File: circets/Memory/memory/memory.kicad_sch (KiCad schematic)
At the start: 29 parts

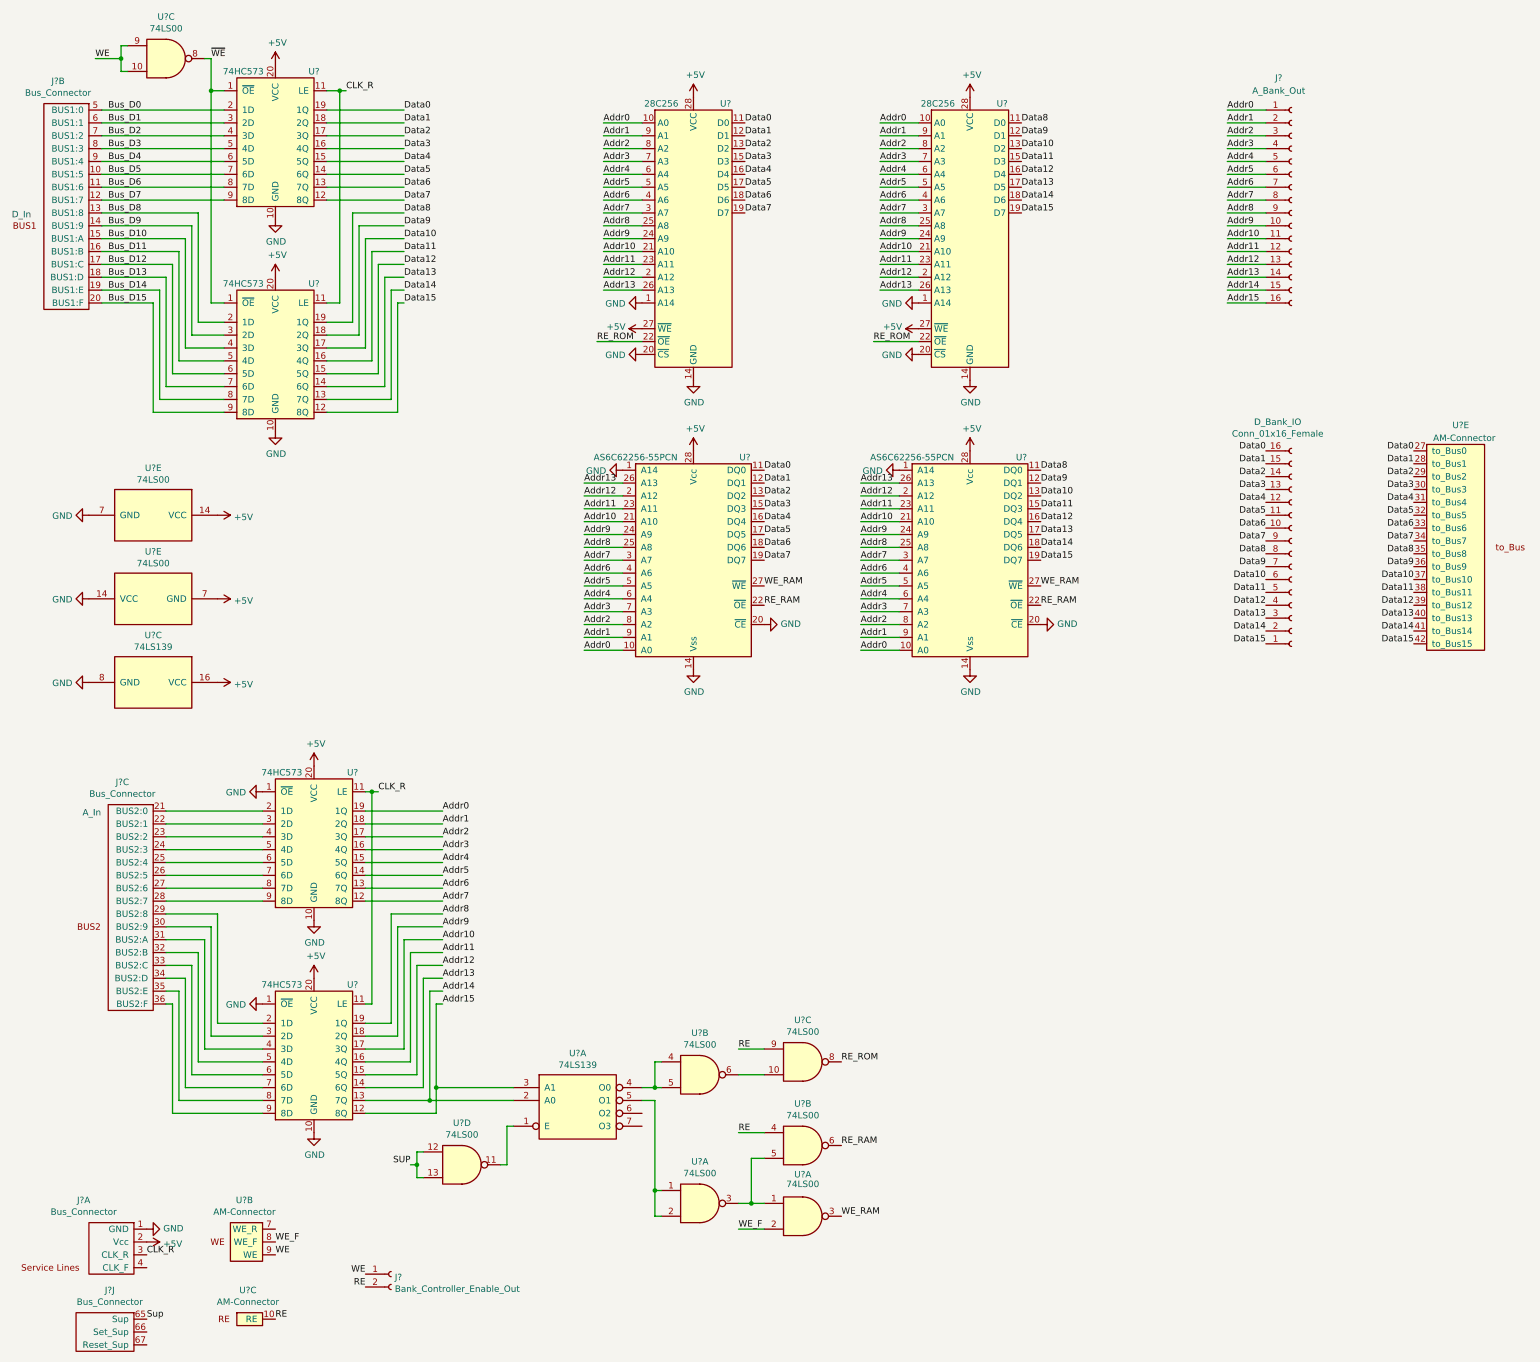
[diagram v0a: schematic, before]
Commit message: Build PCB Layout for Memory Module
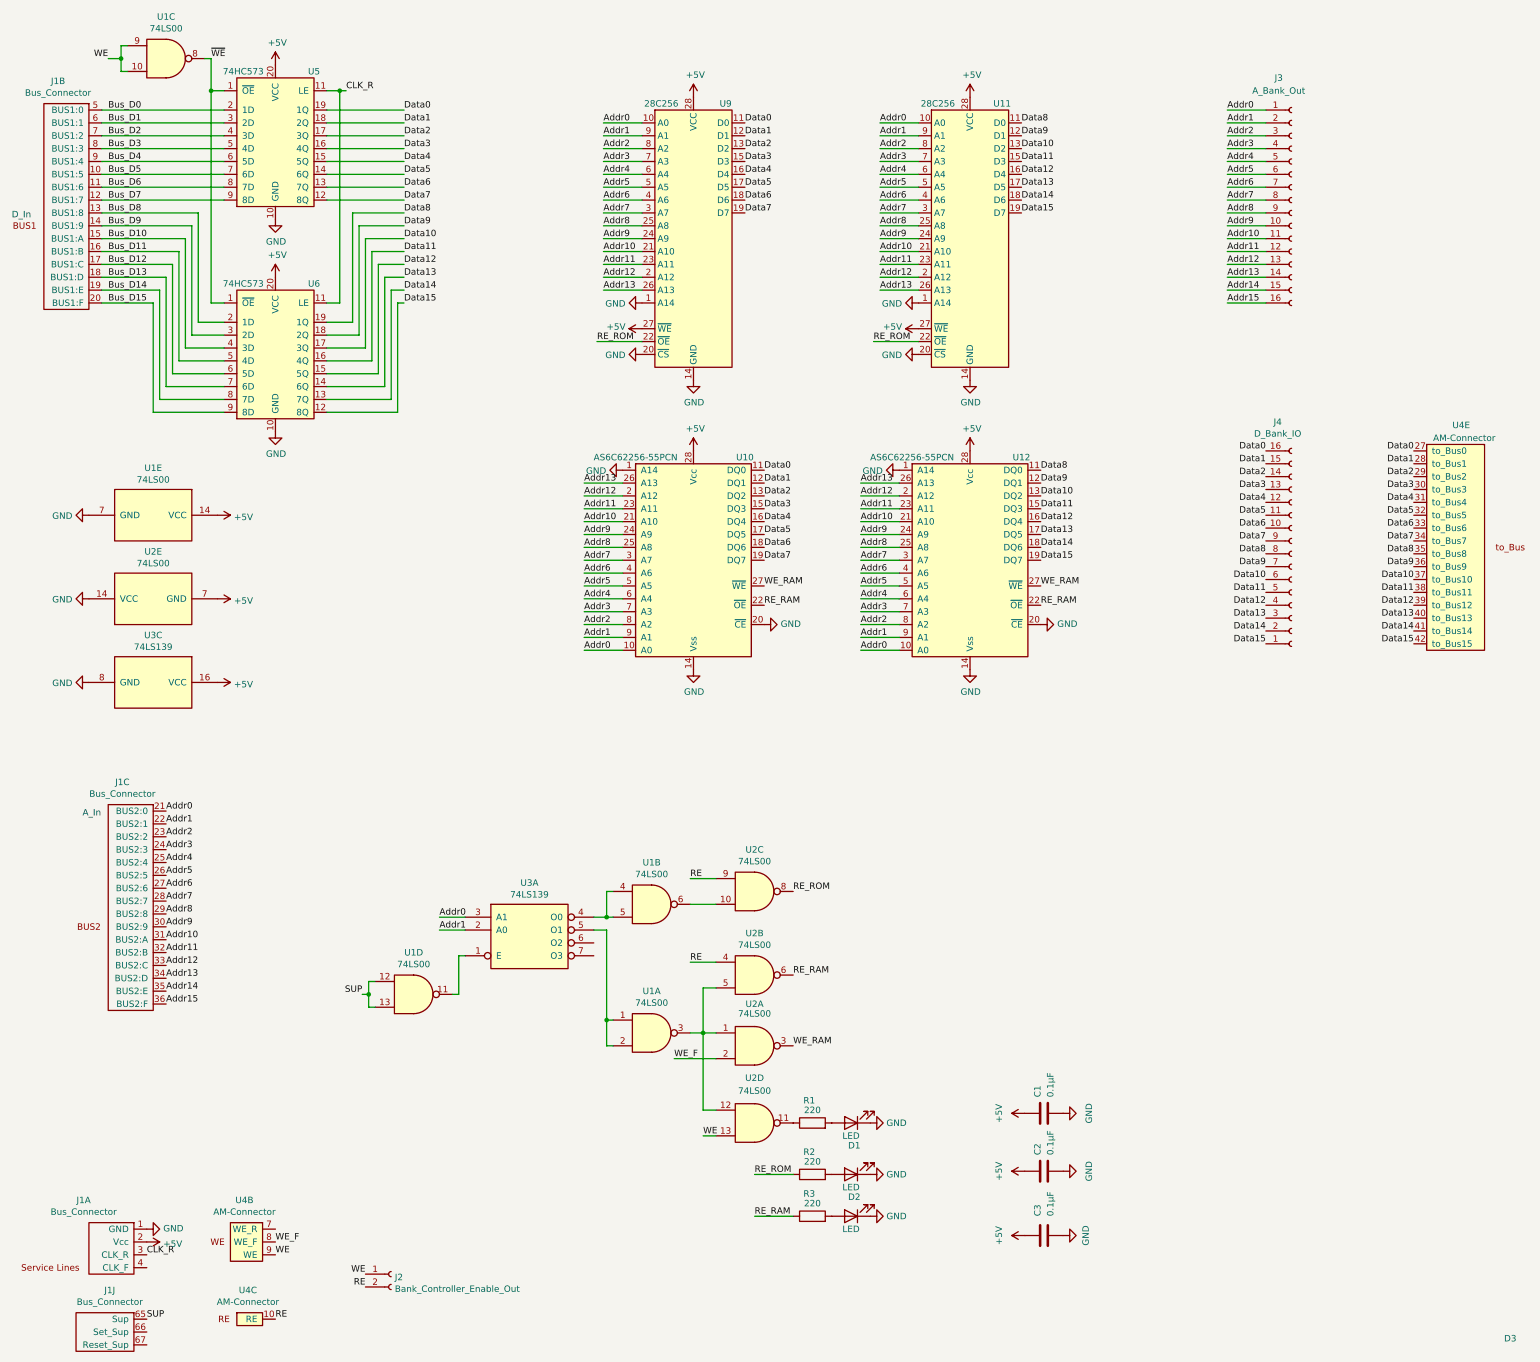
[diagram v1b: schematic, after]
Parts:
- removed U? (x2): 74HC573, symbol Computer_Component_Library:74HC573
- added C1, C2, C3: 0.1µF, Capacitor_THT:C_Disc_D8.0mm_W5.0mm_P5.00mm, symbol Device:C
- added D1, D2, D3: LED, LED_THT:LED_D5.0mm, symbol Device:LED
- added R1, R2, R3: 220, Resistor_THT:R_Axial_DIN0309_L9.0mm_D3.2mm_P2.54mm_Vertical, symbol Device:R
- added unit 4 of U2
- J1: renamed from J?; footprint (none) -> Computer_Component_Library:PinHeader_1x78_P2.54mm_Horizontal
- J2: renamed from J?; footprint (none) -> Connector_PinSocket_2.54mm:PinSocket_1x02_P2.54mm_Horizontal
- J3: renamed from J?; footprint (none) -> Connector_PinSocket_2.54mm:PinSocket_1x16_P2.54mm_Horizontal
- J4: renamed from D_Bank_IO; value Conn_01x16_Female -> D_Bank_IO; footprint (none) -> Connector_PinSocket_2.54mm:PinSocket_1x16_P2.54mm_Horizontal
- U1, U2: renamed from U?; footprint (none) -> Package_DIP:DIP-14_W7.62mm_Socket
- U10, U11, U12, U9: renamed from U?; footprint (none) -> Package_DIP:DIP-28_W15.24mm_Socket
- U3: renamed from U?; footprint (none) -> Package_DIP:DIP-16_W7.62mm_Socket
- U4: renamed from U?; footprint (none) -> Computer_Component_Library:PinHeader_1x42_P2.54mm_Horizontal
- U5, U6: renamed from U?; footprint (none) -> Package_DIP:DIP-20_W7.62mm_Socket
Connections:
- net Sup is gone; now on net SUP: J1.65 (Sup)
- net +5V: now also C1.1, C2.1, C3.1
- net Addr0: now also J1.21 (BUS2:0), U3.3 (A1)
- net Addr1: now also J1.22 (BUS2:1), U3.2 (A0)
- net Addr10: now also J1.31 (BUS2:A)
- net Addr11: now also J1.32 (BUS2:B)
- net Addr12: now also J1.33 (BUS2:C)
- net Addr13: now also J1.34 (BUS2:D)
- net Addr14: now also J1.35 (BUS2:E); no longer U3.2 (A0)
- net Addr15: now also J1.36 (BUS2:F); no longer U3.3 (A1)
- net Addr2: now also J1.23 (BUS2:2)
- net Addr3: now also J1.24 (BUS2:3)
- net Addr4: now also J1.25 (BUS2:4)
- net Addr5: now also J1.26 (BUS2:5)
- net Addr6: now also J1.27 (BUS2:6)
- net Addr7: now also J1.28 (BUS2:7)
- net Addr8: now also J1.29 (BUS2:8)
- net Addr9: now also J1.30 (BUS2:9)
- net GND: now also C1.2, C2.2, C3.2, D1.1 (K), D2.1 (K), D3.1 (K)
- net RE_RAM: now also R3.1
- net RE_ROM: now also R2.1
- net WE: now also U2.13
- net at U1.3, U2.1, U2.5: now also U2.12
- new net: D2.2 (A), R2.2
- new net: R1.1, U2.11
- new net: D3.2 (A), R3.2
- new net: D1.2 (A), R1.2
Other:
- moved on the sheet: U1A, U1B, U1D, U2A, U2B, U2C, U3A
